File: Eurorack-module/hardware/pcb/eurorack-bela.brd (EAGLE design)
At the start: 54.6 x 85 mm, 44 parts, among them IC1 4051B, IC2 4051B, IC3 4051B, IC4 4051B, IC5 4051B, IC6 4051B, IC7 4051B, IC8 4051B, J1 2534-, J2 2534-

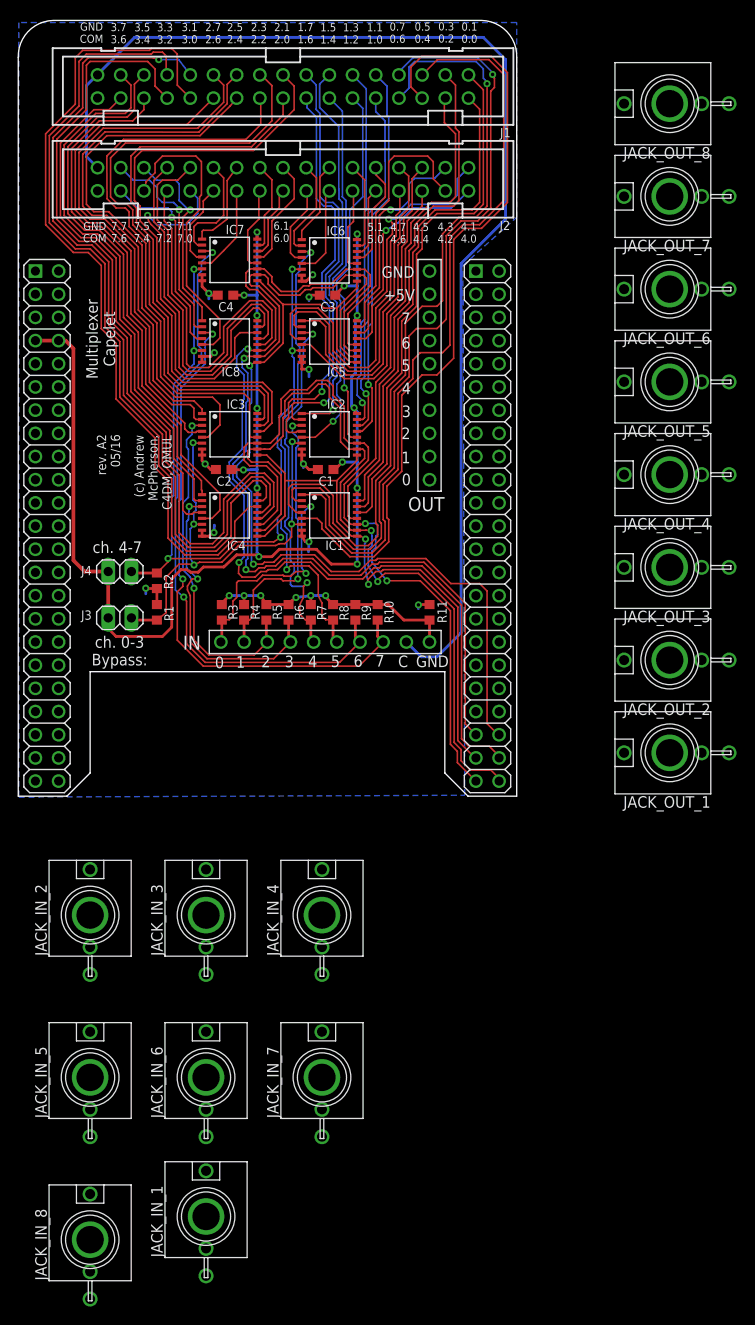
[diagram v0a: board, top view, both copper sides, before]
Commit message: Module updates
Examples also updated.
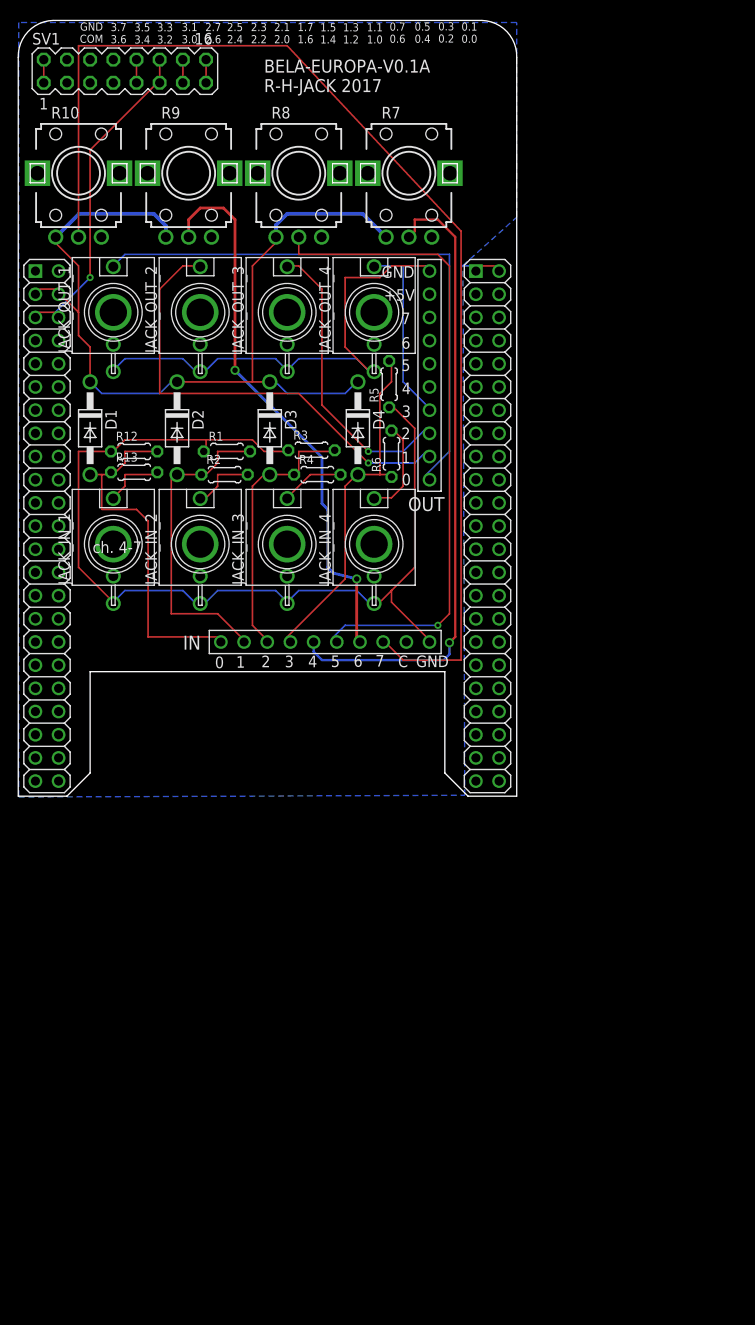
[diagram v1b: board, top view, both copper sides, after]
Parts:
- removed C1, C2, C3, C4: (no value), resistor:C0603
- removed IC1, IC2, IC3, IC4, IC5, IC6, IC7, IC8: 4051B, custom:TSSOP16-PW
- removed J1, J2: 2534-, con-3m:PAK100/2500-34
- removed J3, J4: (no value), pinhead:1X02
- removed JACK_IN_5, JACK_IN_6, JACK_IN_7, JACK_IN_8, JACK_OUT_5, JACK_OUT_6, JACK_OUT_7, JACK_OUT_8: WQP_PJ301M-12_JACKWQP_PJ301M-12_JACK, thonkiconn_eagle_v5:JACK-3.5
- removed R11: 0, rcl:R0603
- added D1, D2, D3, D4: 1N4004, diode:DO41-10
- added R12, R13: 1K, resistor:0204/5
- added SV1: (no value), con-lstb:MA08-2
- R1, R2, R3, R4, R5, R6: value (none) -> 1K; device rcl:R0603 -> resistor:0204/5
- R10, R7, R8, R9: value (none) -> EVUF2A; device rcl:R0603 -> pot:EVUF
- moved JACK_OUT_1 77.8 mm to (-68.6, 83.8), turned to 0 degrees
- moved JACK_IN_1 74.4 mm to (-68.6, 58.4)
- moved JACK_OUT_2 64.0 mm to (-59.1, 83.8), turned to 0 degrees
- moved R10 58.2 mm to (-72.4, 99.1), turned to 0 degrees
- moved R9 51.5 mm to (-60.3, 99.1), turned to 0 degrees
- moved JACK_OUT_3 50.4 mm to (-49.5, 83.8), turned to 0 degrees
- moved R7 49.3 mm to (-36.2, 99.1), turned to 0 degrees
- moved R8 48.3 mm to (-48.3, 99.1), turned to 0 degrees
- moved JACK_IN_2 42.4 mm to (-59.1, 58.4)
- moved JACK_IN_3 41.6 mm to (-49.5, 58.4)
- moved JACK_IN_4 41.0 mm to (-40.0, 58.4)
- moved JACK_OUT_4 36.9 mm to (-40.0, 83.8), turned to 0 degrees
- moved R5 28.4 mm to (-38.4, 75.9), turned to 90 degrees
- moved R6 20.7 mm to (-38.1, 68.3), turned to 90 degrees
- moved R3 20.3 mm to (-46.9, 68.7), turned to 0 degrees
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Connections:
- removed net IN8: JACK_IN_8.P$1
- removed net J2: IC7.15, J2.19
- removed net MUX1INH: IC1.6, IC2.6, IC3.6, IC4.6, J3.2, R1.2
- removed net MUX2INH: IC5.6, IC6.6, IC7.6, IC8.6, J4.2, R2.2
- removed net N$1: IC6.13, J2.9
- removed net N$10: IC5.14, J2.2
- removed net N$11: IC5.15, J2.3
- removed net N$12: IC5.12, J2.4
- removed net N$13: IC5.1, J2.5
- removed net N$14: IC5.5, J2.6
- removed net N$15: IC5.2, J2.7
- removed net N$16: IC5.4, J2.8
- removed net N$17: IC7.13, J2.17
- removed net N$18: IC7.14, J2.18
- removed net N$2: IC6.14, J2.10
- removed net N$20: IC7.12, J2.20
- removed net N$21: IC7.1, J2.21
- removed net N$22: IC7.5, J2.22
- removed net N$23: IC7.2, J2.23
- removed net N$24: IC7.4, J2.24
- removed net N$25: IC8.13, J2.25
- removed net N$26: IC8.14, J2.26
- removed net N$27: IC8.15, J2.27
- removed net N$28: IC8.12, J2.28
- removed net N$29: IC8.1, J2.29
- removed net N$3: IC6.15, J2.11
- removed net N$30: IC8.5, J2.30
- removed net N$31: IC8.2, J2.31
- removed net N$32: IC8.4, J2.32
- removed net N$33: IC1.13, J1.1
- removed net N$34: IC1.14, J1.2
- removed net N$35: IC1.15, J1.3
- removed net N$36: IC1.12, J1.4
- removed net N$37: IC1.1, J1.5
- removed net N$38: IC1.5, J1.6
- removed net N$39: IC1.2, J1.7
- removed net N$4: IC6.12, J2.12
- removed net N$40: IC1.4, J1.8
- removed net N$41: IC2.13, J1.9
- removed net N$42: IC2.14, J1.10
- removed net N$43: IC2.15, J1.11
- removed net N$44: IC2.12, J1.12
- removed net N$45: IC2.1, J1.13
- removed net N$46: IC2.5, J1.14
- removed net N$47: IC2.2, J1.15
- removed net N$48: IC2.4, J1.16
- removed net N$49: IC3.13, J1.17
- removed net N$5: IC6.1, J2.13
- removed net N$50: IC3.14, J1.18
- removed net N$51: IC3.15, J1.19
- removed net N$52: IC3.12, J1.20
- removed net N$53: IC3.1, J1.21
- removed net N$54: IC3.5, J1.22
- removed net N$55: IC3.2, J1.23
- removed net N$56: IC3.4, J1.24
- removed net N$57: IC4.13, J1.25
- removed net N$58: IC4.14, J1.26
- removed net N$59: IC4.15, J1.27
- removed net N$6: IC6.5, J2.14
- removed net N$60: IC4.12, J1.28
- removed net N$61: IC4.1, J1.29
- removed net N$62: IC4.5, J1.30
- removed net N$63: IC4.2, J1.31
- removed net N$64: IC4.4, J1.32
- removed net N$7: IC6.2, J2.15
- removed net N$8: IC6.4, J2.16
- removed net N$9: IC5.13, J2.1
- removed net VDD_3V3EXP: U$1.49, U$1.50
- removed net VDD_5V: U$1.51, U$1.52
- new net +12V: SV1.10, SV1.9
- new net -12V: SV1.1, SV1.2
- new net 1: JACK_IN_1.P$1, R13.2
- new net 2: JACK_IN_2.P$1, R2.2
- new net 3: JACK_IN_3.P$1, R4.2
- new net 3V3: D1.C, D2.C, D3.C, D4.C, R10.1, R7.1, R8.1, R9.1, U$1.49, U$1.50
- new net 4: JACK_IN_4.P$1, R6.2
- new net CV: SV1.13, SV1.14
- new net GATE: SV1.15, SV1.16
- new net SYS_5V: U$1.53
- net +5V: now also SV1.11, SV1.12, U$1.51, U$1.52; no longer C1.1, C2.1, C3.1, C4.1, IC1.16, IC2.16, IC3.16, IC4.16, IC5.16, IC6.16, IC7.16, IC8.16, J3.1, J4.1, U$1.53, U$1.54
- net GND: now also R10.3, R7.3, R8.3, R9.3, SV1.3, SV1.4, SV1.5, SV1.6, SV1.7, SV1.8; no longer C1.2, C2.2, C3.2, C4.2, IC1.7, IC1.8, IC2.7, IC2.8, IC3.7, IC3.8, IC4.7, IC4.8, IC5.7, IC5.8, IC6.7, IC6.8, IC7.7, IC7.8, IC8.7, IC8.8, J1.34, J2.34, R1.1, R11.2, R2.1
- net IN0: now also D1.A, R12.2, R13.1; no longer IC1.3, R3.2
- net IN1: now also D2.A, R1.2, R2.1; no longer IC2.3, JACK_IN_1.P$1, R4.2
- net IN2: now also D3.A, R3.2, R4.1; no longer IC3.3, JACK_IN_2.P$1, R5.2
- net IN3: now also D4.A, R5.2, R6.1; no longer IC4.3, JACK_IN_3.P$1, R6.2
- net IN4: no longer IC5.3, JACK_IN_4.P$1
- net IN5: no longer IC6.3, JACK_IN_5.P$1
- net IN6: no longer IC7.3, JACK_IN_6.P$1
- net IN7: no longer IC8.3, JACK_IN_7.P$1
- net IN_COM: no longer J1.33, J2.33
- net IN_GND: now also R1.1, R12.1; no longer JACK_IN_5.P$3, JACK_IN_6.P$3, JACK_IN_7.P$3, JACK_IN_8.P$3, R10.1, R11.1, R4.1, R6.1, R7.1, R8.1, R9.1
- net MUX1A: no longer IC1.11, IC2.11, IC3.11, IC4.11
- net MUX1B: no longer IC1.10, IC2.10, IC3.10, IC4.10
- net MUX1C: no longer IC1.9, IC2.9, IC3.9, IC4.9
- net MUX2A: no longer IC5.11, IC6.11, IC7.11, IC8.11
- net MUX2B: no longer IC5.10, IC6.10, IC7.10, IC8.10
- net MUX2C: no longer IC5.9, IC6.9, IC7.9, IC8.9
- net OUT5: no longer JACK_OUT_5.P$1
- net OUT6: no longer JACK_OUT_6.P$1
- net OUT7: no longer JACK_OUT_7.P$1
- net OUT8: no longer JACK_OUT_8.P$1
- net OUT_GND: no longer JACK_OUT_5.P$3, JACK_OUT_6.P$3, JACK_OUT_7.P$3, JACK_OUT_8.P$3
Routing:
- net IN_COM: track 131.2 -> 0.00 mm
- net +5V: track 163.1 -> 37.7 mm, vias 14 -> 1
- net MUX2A: track 115.1 -> 0.00 mm, vias 2 -> 0
- net MUX2B: track 107.4 -> 0.00 mm, vias 2 -> 0
- net 3V3: track 0.00 -> 103.1 mm
- net MUX2C: track 98.5 -> 0.00 mm, vias 2 -> 0
- net N$57: track 93.0 -> 0.00 mm, vias 1 -> 0
- net N$60: track 92.4 -> 0.00 mm
- net N$58: track 91.6 -> 0.00 mm
- net N$59: track 91.1 -> 0.00 mm
- net N$40: track 89.6 -> 0.00 mm, vias 1 -> 0
- net MUX1B: track 87.7 -> 0.00 mm, vias 2 -> 0
- net N$39: track 87.6 -> 0.00 mm, vias 1 -> 0
- net N$38: track 87.0 -> 0.00 mm
- net MUX2INH: track 85.6 -> 0.00 mm, vias 6 -> 0
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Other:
- board text added: "BELA-EUROPA-V0.1A R-H-JACK 2017"
- board text removed: "(c) Andrew McPherson, C4DM, QMUL"
- board text removed: "4.1 4.0"
- board text removed: "4.3 4.2"
- board text removed: "4.5 4.4"
- board text removed: "4.7 4.6"
- board text removed: "5.1 5.0"
- board text removed: "6.1 6.0"
- board text removed: "7.1 7.0"
- board text removed: "7.3 7.2"
- board text removed: "7.5 7.4"
- board text removed: "7.7 7.6"
- board text removed: "Bypass:"
- board text removed: "Multiplexer Capelet"
- board text removed: "ch. 0-3"
- board text removed: "rev. A2 05/16"
